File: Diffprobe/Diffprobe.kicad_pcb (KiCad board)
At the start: 4 copper layers, 100 x 28.6 mm, 95 parts, among them J1 Conn_Coaxial, P1 USB_C_Plug_USB2.0, U1 ADA4817-2, U2 LTC6228xS6, U3 LT3032, U4 LM2776, U5 SY6926

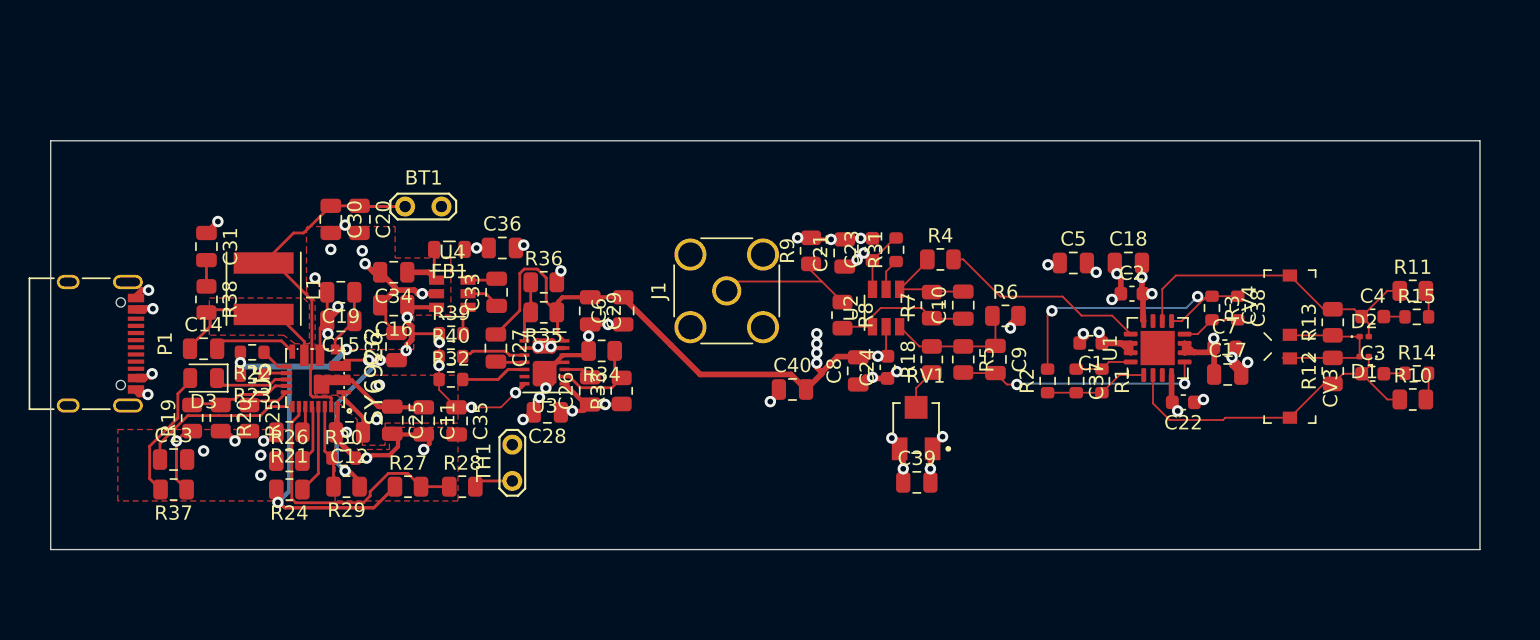
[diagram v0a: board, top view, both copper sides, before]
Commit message: readme, 3d files, measurements and more added
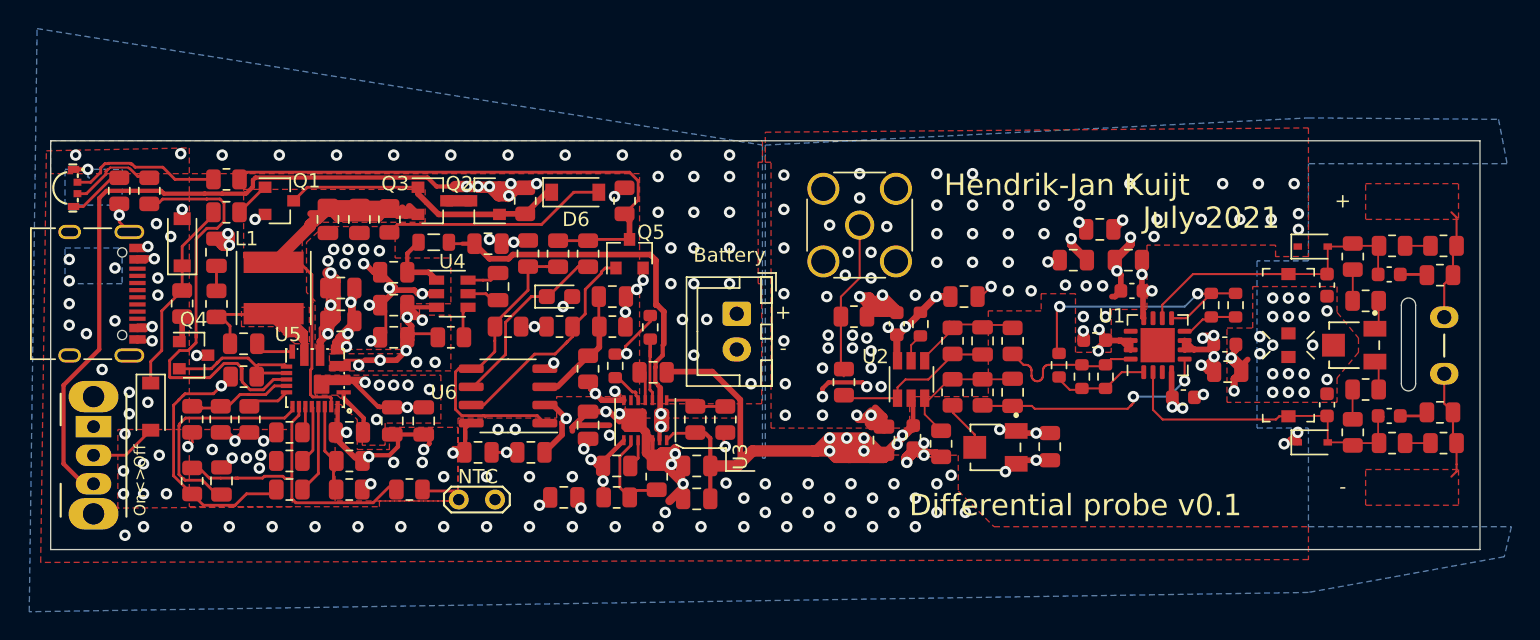
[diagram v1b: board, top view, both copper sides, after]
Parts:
- added C41: 10u, Capacitor_Tantalum_SMD:CP_EIA-2012-15_AVX-P, F.Cu at (115.6, 42.3)
- added C42: 100n, Capacitor_SMD:C_0805_2012Metric, F.Cu at (119.3, 42.3)
- added C43: 100n, Capacitor_SMD:C_0805_2012Metric, F.Cu at (113.6, 53.2)
- added C44: 100n, Capacitor_SMD:C_0805_2012Metric, F.Cu at (109.9, 53.2)
- added C45: DNP, Capacitor_SMD:C_0603_1608Metric, F.Cu at (169.3, 49.9)
- added C46: DNP, Capacitor_SMD:C_0603_1608Metric, F.Cu at (169.3, 41.5)
- added D4: 1N4148W, Diode_SMD:D_SOD-123, F.Cu at (87.0, 50.0)
- added D5: 1N4148W, Diode_SMD:D_SOD-123, F.Cu at (89.2, 38.5)
- added D6: 1N4148W, Diode_SMD:D_SOD-123, F.Cu at (116.7, 35.0)
- added J2: Conn_01x02_Female, custom_coms:probepads, F.Cu at (177.5, 47.7)
- added Q1: MMBT3904, Package_TO_SOT_SMD:SOT-23, F.Cu at (96.0, 35.6)
- added Q2: DMG3415, Package_TO_SOT_SMD:SOT-23, F.Cu at (110.4, 35.6)
- added Q3: DMG3415, Package_TO_SOT_SMD:SOT-23, F.Cu at (106.7, 35.6)
- added Q4: DMG3415, Package_TO_SOT_SMD:SOT-23, F.Cu at (90.0, 46.4)
- added Q5: MMBT3904, Package_TO_SOT_SMD:SOT-23, F.Cu at (120.5, 39.3)
- added R16: 22K, Resistor_SMD:R_0805_2012Metric, F.Cu at (92.3, 36.4)
- added R17: 100K, Resistor_SMD:R_0805_2012Metric, F.Cu at (103.7, 36.9)
- added R41: 100K, Resistor_SMD:R_0805_2012Metric, F.Cu at (113.2, 35.6)
- added R42: 22K, Resistor_SMD:R_0805_2012Metric, F.Cu at (89.2, 42.8)
- added R43: 100K, Resistor_SMD:R_0805_2012Metric, F.Cu at (93.5, 47.9)
- added R44: 33K, Resistor_SMD:R_0805_2012Metric, F.Cu at (117.6, 47.4)
- added R45: 47K, Resistor_SMD:R_0805_2012Metric, F.Cu at (119.3, 44.4)
- added R46: 27K, Resistor_SMD:R_0805_2012Metric, F.Cu at (112.0, 44.4)
- added R47: 47K, Resistor_SMD:R_0805_2012Metric, F.Cu at (113.4, 39.3)
- added R48: 47K, Resistor_SMD:R_0805_2012Metric, F.Cu at (117.6, 39.3)
- added R49: 10K, Resistor_SMD:R_0805_2012Metric, F.Cu at (115.5, 39.3)
- added R50: 47K, Resistor_SMD:R_0805_2012Metric, F.Cu at (115.6, 44.4)
- added R51: 47K, Resistor_SMD:R_0805_2012Metric, F.Cu at (120.2, 35.6)
- added R52: 2Meg, Resistor_SMD:R_0805_2012Metric, F.Cu at (177.4, 52.5)
- added R53: 2Meg, Resistor_SMD:R_0805_2012Metric, F.Cu at (177.4, 38.8)
- added R54: 42.2K, Resistor_SMD:R_0805_2012Metric, F.Cu at (172.0, 48.8)
- added R55: 42.2K, Resistor_SMD:R_0805_2012Metric, F.Cu at (172.0, 42.6)
- added RV2: 500R, custom_coms:TRIM_3313J-1-103E, F.Cu at (171.2, 45.7)
- added SW1: SW_SPDT, Button_Switch_THT:SW_CuK_OS102011MA1QN1_SPDT_Angled, F.Cu at (83.0, 51.4)
- added U6: TS372, Package_SO:SO-8_3.9x4.9mm_P1.27mm, F.Cu at (112.0, 49.2)
- BT1: footprint TestPoint:TestPoint_2Pads_Pitch2.54mm_Drill0.8mm -> Connector_JST:JST_XH_B2B-XH-A_1x02_P2.50mm_Vertical
- D1, D2: footprint Diode_SMD:D_0201_0603Metric -> Diode_SMD:D_SOD-323
- D3: value LED -> LED_ABGR; footprint LED_SMD:LED_0805_2012Metric -> custom_coms:MHS110_RGB
- R10, R11: value 4.5Meg -> 2Meg
- R12, R13: value 500K -> 402K
- R14, R15: value 1K -> 1K tf; footprint Resistor_SMD:R_0603_1608Metric -> Resistor_SMD:R_0805_2012Metric
- R18: value 20K -> 22K
- R22: value 10K -> 2K; footprint Resistor_SMD:R_0603_1608Metric -> Resistor_SMD:R_0805_2012Metric
- R23: value 10K -> 1K; footprint Resistor_SMD:R_0603_1608Metric -> Resistor_SMD:R_0805_2012Metric
- R28: value 4.4K -> 4.42K
- R30, R39: footprint Resistor_SMD:R_0603_1608Metric -> Resistor_SMD:R_0805_2012Metric
- moved BT1 24.4 mm to (128.0, 43.5), turned to 270 degrees
- moved C40 24.2 mm to (153.4, 37.6)
- moved R37 21.0 mm to (86.9, 34.9), turned to 270 degrees
- moved D3 17.2 mm to (81.6, 33.4), turned to 270 degrees
- moved R36 15.9 mm to (127.2, 50.9), turned to 270 degrees
- moved R27 15.1 mm to (89.9, 55.2), turned to 90 degrees
- moved R22 14.6 mm to (84.8, 34.9), turned to 270 degrees
- moved C6 14.1 mm to (125.2, 56.5), turned to 0 degrees
- moved R40 14.1 mm to (122.0, 44.5), turned to 270 degrees
- moved R23 13.8 mm to (92.3, 34.1), turned to 0 degrees
- moved C29 13.2 mm to (125.2, 54.1), turned to 180 degrees
- moved R35 13.0 mm to (125.1, 50.9), turned to 90 degrees
- moved R32 11.5 mm to (119.5, 47.1), turned to 270 degrees
- moved C27 11.1 mm to (122.2, 47.6), turned to 180 degrees
- moved J1 10.4 mm to (136.6, 37.3)
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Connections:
- BT1 pad 1: Net-(BT1-Pad1) -> Battery
- C11 pad 1: Net-(C11-Pad1) -> /Battery management/VUSB
- C12 pad 1: Net-(C11-Pad1) -> /Battery management/VUSB
- C20 pad 1: Net-(BT1-Pad1) -> Net-(C20-Pad1)
- C25 pad 1: Net-(C11-Pad1) -> /Battery management/VUSB
- C30 pad 1: Net-(BT1-Pad1) -> Net-(C20-Pad1)
- CV3 pad 1: Net-(CV1-Pad1) -> GND
- CV4 pad 1: Net-(CV1-Pad1) -> GND
- D1 pad 1: Net-(C3-Pad1) -> GND
- D1 pad 2: Net-(CV1-Pad1) -> Net-(C3-Pad1)
- D2 pad 1: Net-(CV1-Pad1) -> GND
- D3 pad 1: Net-(D3-Pad1) -> /Battery management/BUS
- L1 pad 1: Net-(BT1-Pad1) -> Net-(C20-Pad1)
- P1 pad A4: Net-(C11-Pad1) -> /Battery management/VUSB
- P1 pad A9: Net-(C11-Pad1) -> /Battery management/VUSB
- P1 pad B4: Net-(C11-Pad1) -> /Battery management/VUSB
- P1 pad B9: Net-(C11-Pad1) -> /Battery management/VUSB
- R10 pad 2: /IN- -> Net-(R10-Pad2)
- R11 pad 2: /IN+ -> Net-(R11-Pad2)
- R12 pad 2: Net-(CV1-Pad1) -> Net-(R12-Pad2)
- R13 pad 1: Net-(CV1-Pad1) -> Net-(R13-Pad1)
- R19 pad 1: Net-(C11-Pad1) -> /Battery management/VUSB
- R22 pad 1: Net-(R22-Pad1) -> Net-(D3-Pad4)
- R22 pad 2: /Battery management/BUS -> GND
- R23 pad 1: Net-(R23-Pad1) -> Net-(D3-Pad2)
- R23 pad 2: /Battery management/BUS -> Bat_Indicator
- R37 pad 1: Net-(C11-Pad1) -> Net-(D3-Pad3)
- R37 pad 2: Net-(D3-Pad2) -> Net-(R37-Pad2)
- U5 pad 1: Net-(C11-Pad1) -> /Battery management/VUSB
- U5 pad 10: Net-(D3-Pad1) -> Net-(R37-Pad2)
- U5 pad 19: Net-(BT1-Pad1) -> Net-(C20-Pad1)
- U5 pad 2: Net-(C11-Pad1) -> /Battery management/VUSB
- U5 pad 8: Net-(R22-Pad1) -> /Battery management/Enable
- U5 pad 9: Net-(R23-Pad1) -> /Battery management/Enable
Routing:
- net GND: track 65.6 -> 140.2 mm, vias 39 -> 240
- net Battery: track 0.00 -> 67.8 mm, vias 0 -> 7
- net Net-(R37-Pad2): track 0.00 -> 42.8 mm
- net Net-(C20-Pad1): track 0.00 -> 40.4 mm
- net Bat_Indicator: track 0.00 -> 38.5 mm
- net Net-(BT1-Pad1): track 26.0 -> 0.00 mm
- net -VDC: track 3.26 -> 28.6 mm, vias 3 -> 2
- net Net-(R46-Pad2): track 0.00 -> 23.0 mm
- net Net-(C11-Pad1): track 20.7 -> 0.00 mm, vias 5 -> 0
- net Net-(D6-Pad1): track 0.00 -> 20.6 mm
- net /Battery management/VUSB: track 0.00 -> 19.6 mm, vias 0 -> 11
- net Net-(D6-Pad2): track 0.00 -> 15.8 mm
- net Net-(Q5-Pad1): track 0.00 -> 15.7 mm
- net Net-(D4-Pad1): track 0.00 -> 13.9 mm
- net -5V: track 57.7 -> 71.3 mm, vias 10 -> 14
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- added copper zone on In2.Cu, net /Battery management/BUS
- added copper zone on B.Cu, net /Battery management/VUSB
- added copper zone on F.Cu, net /Battery management/VUSB
- added copper zone on In2.Cu, net /Battery management/VUSB
- added copper zone on F.Cu, net /IN+
- added copper zone on F.Cu, net /IN-
- added copper zone on In2.Cu, net Battery
- added copper zone on B.Cu, net GND
- added copper zone on F.Cu, net Net-(C20-Pad1)
- added copper zone on F.Cu, net VDC
- removed copper zone on In2.Cu, net -VDC
- removed copper zone on F.Cu, net Net-(C11-Pad1)
- removed copper zone on In2.Cu, net Net-(C11-Pad1)
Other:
- outline, holes or cut-outs redrawn
- net class Microstrip added: clearance 0.2, trace_width 0.147, via_dia 0.8, via_drill 0.4
- board text added: "+"
- board text added: "-"
- board text added: "Battery"
- board text added: "Differential probe v0.1"
- board text added: "GND"
- board text added: "Hendrik-Jan Kuijt"
- board text added: "July 2021"
- board text added: "NTC"
- board text added: "On<>Off"
- board text added: "VUSB"
